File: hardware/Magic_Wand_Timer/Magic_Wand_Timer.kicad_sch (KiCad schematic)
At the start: 21 parts, among them J1 Conn_01x03, J2 Conn_01x03, J3 Conn_01x03, J4 Conn_01x02, Q1 AS2302, U1 MPM3610GQV-Z, U2 NE555D

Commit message: adding vias to a couple of PCBs, magic wand PCB changes
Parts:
- removed J1, J2, J3: Conn_01x03, Useful Modifications:JST_XH_B3B-XH-A_1x03_P2.54mm_Vertical, symbol Connector_Generic:Conn_01x03
- removed R3: 100K, Resistor_SMD:R_0805_2012Metric, symbol Device:R_Small
- removed U1: MPM3610GQV-Z, QFN3p0x5p0x1p6_MPM3610_MNP, symbol Magic_Wand_Timer:MPM3610GQV-Z
- added J1: Action Input, Connector_JST:JST_XH_B4B-XH-A_1x04_P2.50mm_Vertical, symbol Connector:Conn_01x04_Pin
- added J2: Caddy In/Out, Connector_JST:JST_XH_B4B-XH-A_1x04_P2.50mm_Vertical, symbol Connector:Conn_01x04_Pin
- added Q2: SI2301CDS-T1-GE3, Package_TO_SOT_SMD:SOT-23, symbol Transistor_FET:Si2371EDS
- added R7, R8: 100K, Resistor_SMD:R_0805_2012Metric, symbol Device:R_Small
- C1: MPN (none) -> C1710
- C2: value 10uF -> 10nF; MPN (none) -> C1710
- C3: value 22uF -> 1uF; MPN (none) -> C28323
- C4: MPN (none) -> C15850
- D1: value 1N4448W -> 1N4148W; MPN (none) -> C81598
- J4: symbol Connector_Generic:Conn_01x02 -> Connector:Conn_01x02_Pin
- Q1: MPN (none) -> C20917
- R1: value 100K -> 10K; MPN (none) -> C17414
- R2: value 19.1K -> 1K; MPN (none) -> C11702
- R4, R6: MPN (none) -> C17414
- R5: MPN (none) -> C149504
- U2: MPN (none) -> C7593
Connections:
- net +12V: now also J1.1 (Pin_1), J2.1 (Pin_1); no longer C2.1
- net +5V: now also J1.2 (Pin_2), J2.2 (Pin_2), Q2.2 (S), R8.1; no longer C3.1, R1.1
- net GND: now also C2.1, C3.1, J1.3 (Pin_3), J2.3 (Pin_3), R7.2; no longer C2.2, C3.2
- net Trigger: now also R1.1, R2.1, J1.4 (Pin_4); no longer R4.2, U2.2 (TR)
- net Filtered_Input: now reaches R1.2
- net Filtered_Input: now also C2.2, C3.2, R4.2, U2.2 (TR); no longer R2.1
- net at R2.2: now also Q2.1 (G), R8.2
- new net Caddy_Trigger: J2.4 (Pin_4), Q2.3 (D), R7.1
- no-connect marks 2 -> 1
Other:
- note removed: "DC-DC Converter"
- moved on the sheet: C1, C4, H1, H2, R4, R5, RV1, U2

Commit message: magic wand PCB updates
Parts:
- R1: renamed from R2; MPN C11702 -> C17513
- R4: value 10K -> 100K; MPN C17414 -> C149504
- renumbered C3 to C2, C2 to C3, J4 to J3, Q2 to Q1, Q1 to Q2, R8 to R2, R7 to R3, R1 to R5, R5 to R6, R6 to R7, U2 to U1
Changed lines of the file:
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@@
   (symbol (lib_id "Device:R_Small") (at 214.63 128.27 0) (unit 1)
     (in_bom yes) (on_board yes) (dnp no) (fields_autoplaced)
-    (property "Reference" "R6" (at 217.17 126.9999 0)
+    (property "Reference" "R7" (at 217.17 126.9999 0)
       (effects (font (size 1.27 1.27)) (justify left))
     )
@@
       (project "Magic_Wand_Timer"
         (path "/c5eed718-a5cc-419c-bfa3-9985e5d26a34"
-          (reference "R6") (unit 1)
+          (reference "R7") (unit 1)
         )
       )
@@
   (symbol (lib_id "Device:R_Small") (at 78.74 111.76 0) (unit 1)
     (in_bom yes) (on_board yes) (dnp no) (fields_autoplaced)
-    (property "Reference" "R7" (at 81.28 110.4899 0)
+    (property "Reference" "R3" (at 81.28 110.4899 0)
       (effects (font (size 1.27 1.27)) (justify left))
     )
@@
       (project "Magic_Wand_Timer"
         (path "/c5eed718-a5cc-419c-bfa3-9985e5d26a34"
-          (reference "R7") (unit 1)
+          (reference "R3") (unit 1)
         )
       )
@@
   (symbol (lib_id "Device:R_Small") (at 135.255 50.165 90) (unit 1)
     (in_bom yes) (on_board yes) (dnp no) (fields_autoplaced)
-    (property "Reference" "R1" (at 135.255 45.085 90)
+    (property "Reference" "R5" (at 135.255 45.085 90)
       (effects (font (size 1.27 1.27)))
     )
@@
       (project "Magic_Wand_Timer"
         (path "/c5eed718-a5cc-419c-bfa3-9985e5d26a34"
-          (reference "R1") (unit 1)
+          (reference "R5") (unit 1)
         )
       )
@@
   (symbol (lib_id "Transistor_FET:Si2371EDS") (at 76.2 97.155 0) (mirror x) (unit 1)
     (in_bom yes) (on_board yes) (dnp no)
-    (property "Reference" "Q2" (at 82.55 97.79 0)
+    (property "Reference" "Q1" (at 82.55 97.79 0)
       (effects (font (size 1.27 1.27)) (justify left))
     )
@@
       (project "Magic_Wand_Timer"
         (path "/c5eed718-a5cc-419c-bfa3-9985e5d26a34"
+          (reference "Q1") (unit 1)
+        )
+      )
+    )
+  )
+  (symbol (lib_id "Device:Q_NMOS_GSD") (at 223.52 123.19 0) (unit 1)
+    (in_bom yes) (on_board yes) (dnp no) (fields_autoplaced)
+    (property "Reference" "Q2" (at 229.87 121.9199 0)
+      (effects (font (size 1.27 1.27)) (justify left))
+    )
+    (property "Value" "AS2302" (at 229.87 124.4599 0)
+      (effects (font (size 1.27 1.27)) (justify left))
+    )
+    (property "Footprint" "Package_TO_SOT_SMD:SOT-23" (at 228.6 120.65 0)
+      (effects (font (size 1.27 1.27)) hide)
+    )
+    (property "Datasheet" "https://media.digikey.com/pdf/Data%20Sheets/Anbon%20Semi%20PDFs/AS2302.pdf" (at 223.52 123.19 0)
+      (effects (font (size 1.27 1.27)) hide)
+    )
+    (property "MPN" "C20917" (at 223.52 123.19 0)
+      (effects (font (size 1.27 1.27)) hide)
+    )
+    (pin "1")
+    (pin "2")
+    (pin "3")
+    (instances
+      (project "Magic_Wand_Timer"
+        (path "/c5eed718-a5cc-419c-bfa3-9985e5d26a34"
           (reference "Q2") (unit 1)
-        )
-      )
-    )
-  )
-  (symbol (lib_id "Device:Q_NMOS_GSD") (at 223.52 123.19 0) (unit 1)
-    (in_bom yes) (on_board yes) (dnp no) (fields_autoplaced)
-    (property "Reference" "Q1" (at 229.87 121.9199 0)
-      (effects (font (size 1.27 1.27)) (justify left))
-    )
-    (property "Value" "AS2302" (at 229.87 124.4599 0)
-      (effects (font (size 1.27 1.27)) (justify left))
-    )
-    (property "Footprint" "Package_TO_SOT_SMD:SOT-23" (at 228.6 120.65 0)
-      (effects (font (size 1.27 1.27)) hide)
-    )
-    (property "Datasheet" "https://media.digikey.com/pdf/Data%20Sheets/Anbon%20Semi%20PDFs/AS2302.pdf" (at 223.52 123.19 0)
-      (effects (font (size 1.27 1.27)) hide)
-    )
-    (property "MPN" "C20917" (at 223.52 123.19 0)
-      (effects (font (size 1.27 1.27)) hide)
-    )
-    (pin "1")
-    (pin "2")
-    (pin "3")
-    (instances
-      (project "Magic_Wand_Timer"
-        (path "/c5eed718-a5cc-419c-bfa3-9985e5d26a34"
-          (reference "Q1") (unit 1)
         )
       )
@@
   (symbol (lib_id "Device:R_Small") (at 173.99 91.44 0) (unit 1)
     (in_bom yes) (on_board yes) (dnp no) (fields_autoplaced)
-    (property "Reference" "R5" (at 176.53 90.1699 0)
+    (property "Reference" "R6" (at 176.53 90.1699 0)
       (effects (font (size 1.27 1.27)) (justify left))
     )
@@
       (project "Magic_Wand_Timer"
         (path "/c5eed718-a5cc-419c-bfa3-9985e5d26a34"
-          (reference "R5") (unit 1)
+          (reference "R6") (unit 1)
         )
       )
@@
   (symbol (lib_id "Device:C_Small") (at 143.51 55.88 180) (unit 1)
     (in_bom yes) (on_board yes) (dnp no)
-    (property "Reference" "C3" (at 146.05 55.88 90)
+    (property "Reference" "C2" (at 146.05 55.88 90)
       (effects (font (size 1.27 1.27)))
     )
@@
       (project "Magic_Wand_Timer"
         (path "/c5eed718-a5cc-419c-bfa3-9985e5d26a34"
-          (reference "C3") (unit 1)
+          (reference "C2") (unit 1)
         )
       )
@@
   (symbol (lib_id "Device:C_Small") (at 153.035 55.88 180) (unit 1)
     (in_bom yes) (on_board yes) (dnp no)
-    (property "Reference" "C2" (at 155.575 55.88 90)
+    (property "Reference" "C3" (at 155.575 55.88 90)
       (effects (font (size 1.27 1.27)))
     )
@@
       (project "Magic_Wand_Timer"
         (path "/c5eed718-a5cc-419c-bfa3-9985e5d26a34"
-          (reference "C2") (unit 1)
+          (reference "C3") (unit 1)
         )
       )
@@
   (symbol (lib_id "Device:R_Small") (at 69.85 92.71 0) (unit 1)
     (in_bom yes) (on_board yes) (dnp no)
-    (property "Reference" "R8" (at 65.405 90.805 0)
+    (property "Reference" "R2" (at 65.405 90.805 0)
       (effects (font (size 1.27 1.27)) (justify left))
     )
@@
       (project "Magic_Wand_Timer"
         (path "/c5eed718-a5cc-419c-bfa3-9985e5d26a34"
-          (reference "R8") (unit 1)
+          (reference "R2") (unit 1)
         )
       )
@@
   (symbol (lib_id "Timer:NE555D") (at 143.51 110.49 0) (unit 1)
     (in_bom yes) (on_board yes) (dnp no) (fields_autoplaced)
-    (property "Reference" "U2" (at 145.5294 97.79 0)
-      (effects (font (size 1.27 1.27)) (justify left))
-    )
-    (property "Value" "NE555D" (at 145.5294 100.33 0)
+    (property "Reference" "U1" (at 145.7041 97.79 0)
+      (effects (font (size 1.27 1.27)) (justify left))
+    )
+    (property "Value" "NE555D" (at 145.7041 100.33 0)
       (effects (font (size 1.27 1.27)) (justify left))
     )
@@
       (project "Magic_Wand_Timer"
         (path "/c5eed718-a5cc-419c-bfa3-9985e5d26a34"
-          (reference "U2") (unit 1)
+          (reference "U1") (unit 1)
         )
       )
@@
   (symbol (lib_id "Device:R_Small") (at 62.865 97.155 90) (unit 1)
     (in_bom yes) (on_board yes) (dnp no)
-    (property "Reference" "R2" (at 62.865 99.06 90)
+    (property "Reference" "R1" (at 62.865 99.06 90)
       (effects (font (size 1.27 1.27)))
     )
@@
       (effects (font (size 1.27 1.27)) hide)
     )
-    (property "MPN" "C11702" (at 62.865 97.155 90)
-      (effects (font (size 1.27 1.27)) hide)
-    )
-    (pin "1")
-    (pin "2")
-    (instances
-      (project "Magic_Wand_Timer"
-        (path "/c5eed718-a5cc-419c-bfa3-9985e5d26a34"
-          (reference "R2") (unit 1)
+    (property "MPN" "C17513" (at 62.865 97.155 90)
+      (effects (font (size 1.27 1.27)) hide)
+    )
+    (pin "1")
+    (pin "2")
+    (instances
+      (project "Magic_Wand_Timer"
+        (path "/c5eed718-a5cc-419c-bfa3-9985e5d26a34"
+          (reference "R1") (unit 1)
         )
       )
@@
       (effects (font (size 1.27 1.27)) (justify left))
     )
-    (property "Value" "10K" (at 130.81 100.3299 0)
+    (property "Value" "100K" (at 130.81 100.3299 0)
       (effects (font (size 1.27 1.27)) (justify left))
     )
@@
       (effects (font (size 1.27 1.27)) hide)
     )
-    (property "MPN" "C17414" (at 128.27 99.06 0)
+    (property "MPN" "C149504" (at 128.27 99.06 0)
       (effects (font (size 1.27 1.27)) hide)
     )
@@
   (symbol (lib_id "Connector:Conn_01x02_Pin") (at 233.68 115.57 180) (unit 1)
     (in_bom yes) (on_board yes) (dnp no)
-    (property "Reference" "J4" (at 234.95 114.935 0)
+    (property "Reference" "J3" (at 234.95 114.935 0)
       (effects (font (size 1.27 1.27)) (justify right))
     )
@@
       (project "Magic_Wand_Timer"
         (path "/c5eed718-a5cc-419c-bfa3-9985e5d26a34"
-          (reference "J4") (unit 1)
-        )
-      )
+          (reference "J3") (unit 1)
+        )
+      )

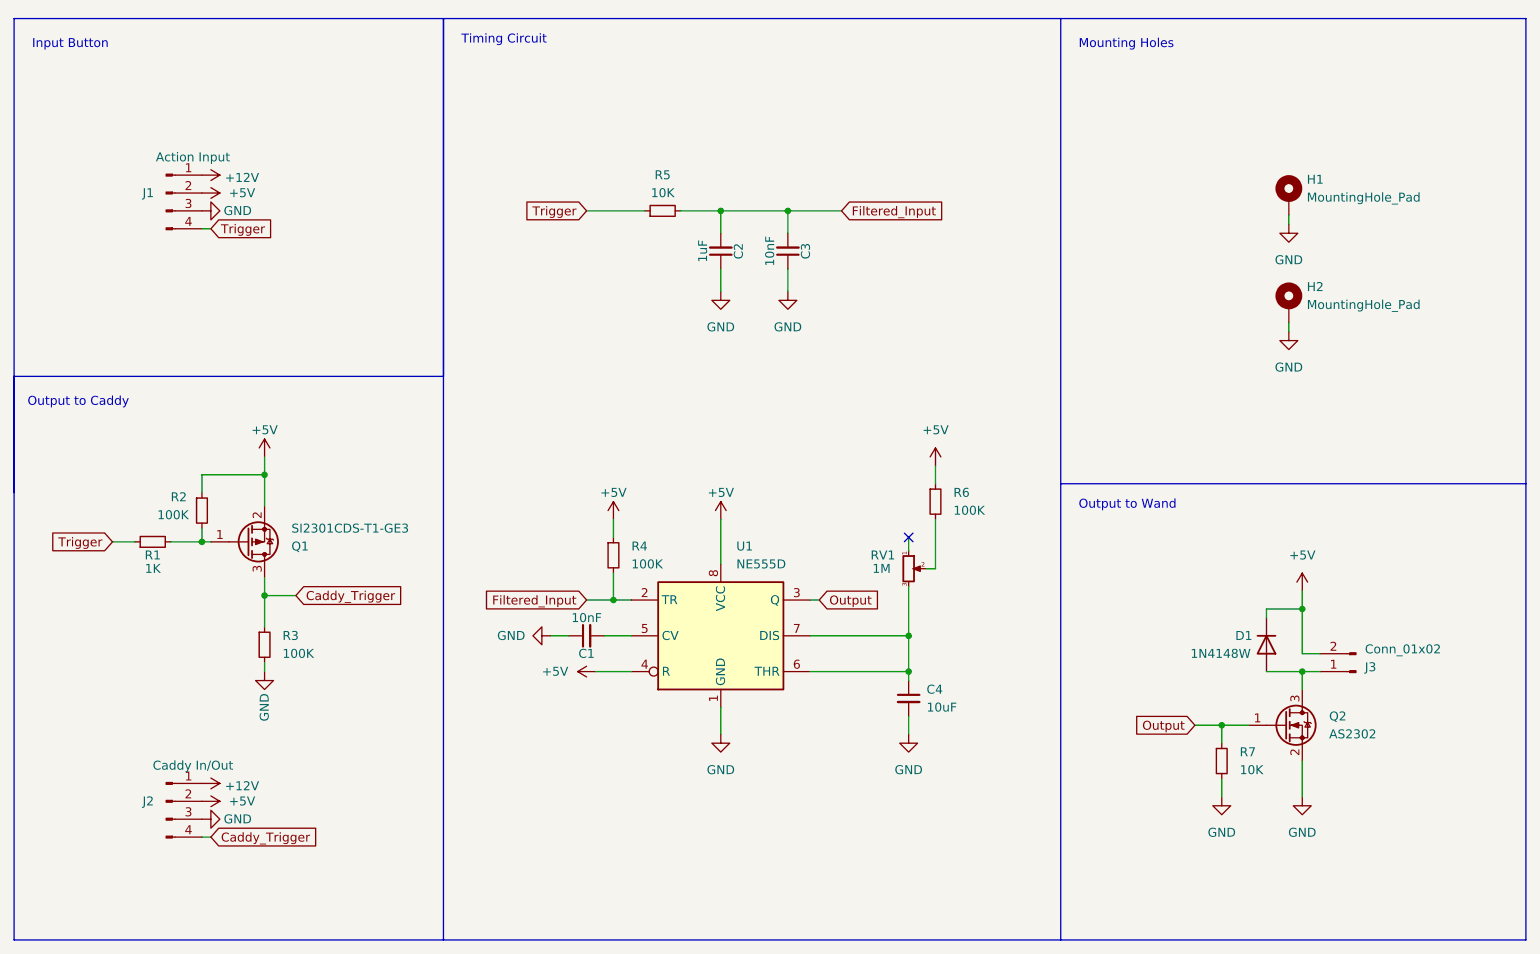
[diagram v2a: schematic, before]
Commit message: Magic Wand Timer Updates
Added 12V/5V switching, SMD/THT potentiometer options, Delayed start to handle erratic comparator behavior
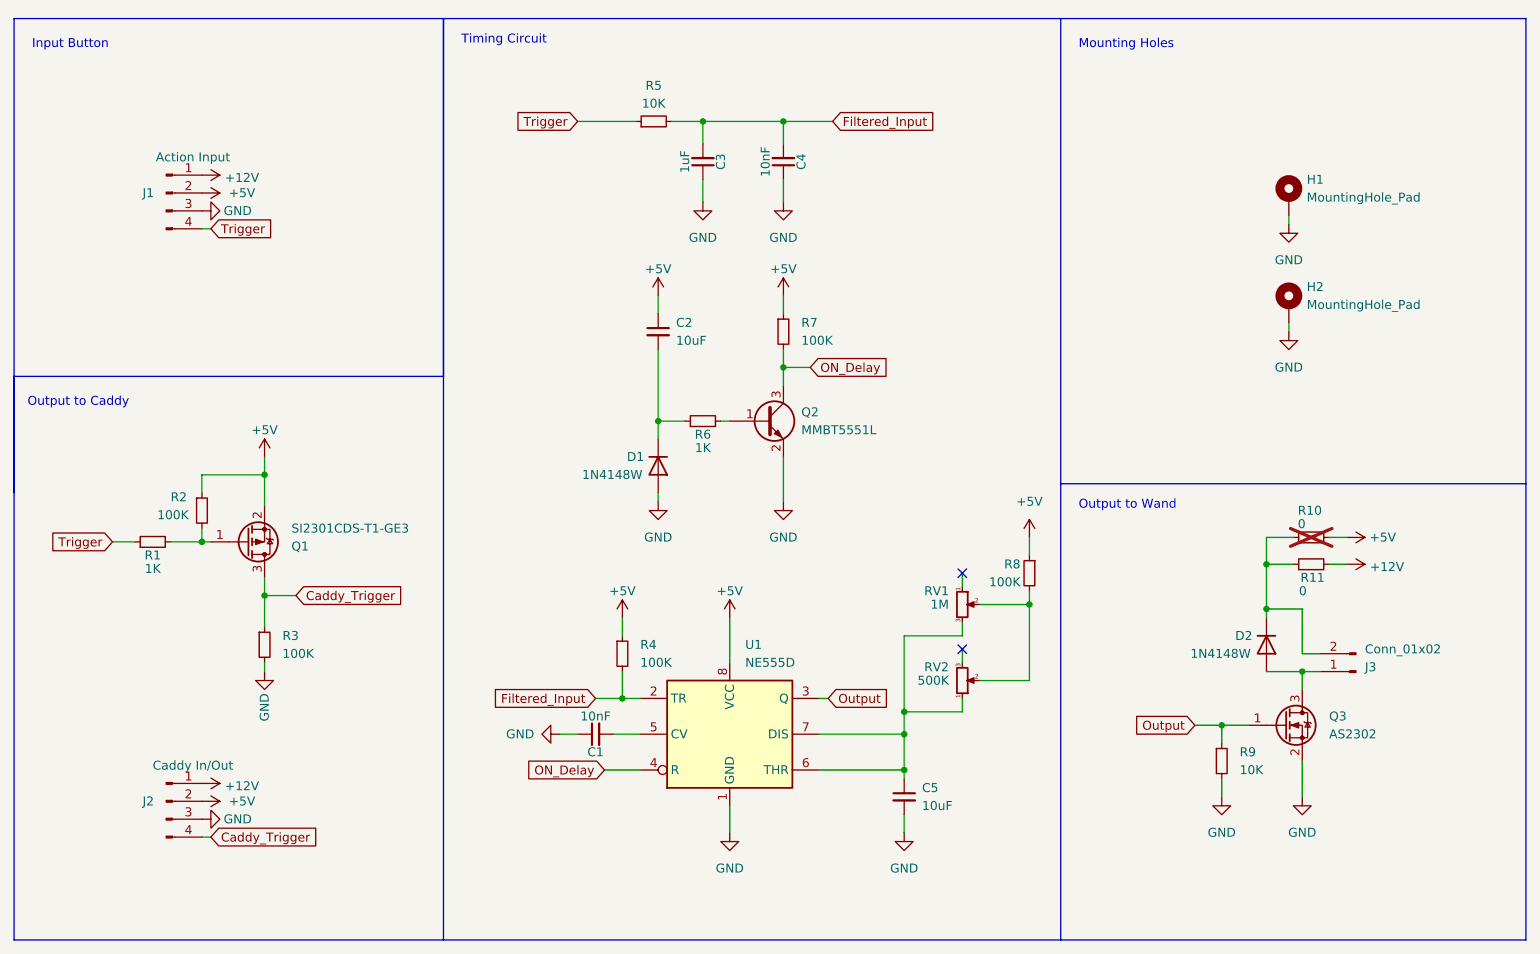
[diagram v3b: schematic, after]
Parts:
- added C2: 10uF, Capacitor_SMD:C_0805_2012Metric, symbol Device:C_Small
- added D1: 1N4148W, Diode_SMD:D_SOD-123, symbol Diode:1N4448W
- added Q2: MMBT5551L, Package_TO_SOT_SMD:SOT-23, symbol Transistor_BJT:MMBT5551L
- added R10, R11: 0, Resistor_SMD:R_0805_2012Metric, symbol Device:R_Small
- added R6: 1K, Resistor_SMD:R_0805_2012Metric, symbol Device:R_Small
- added R7: 100K, Resistor_SMD:R_0805_2012Metric, symbol Device:R_Small
- added RV2: 500K, Potentiometer_SMD:Potentiometer_Bourns_TC33X_Vertical, symbol Device:R_Potentiometer_Small
- renumbered C2 to C3, C3 to C4, C4 to C5, D1 to D2, Q2 to Q3, R6 to R8, R7 to R9
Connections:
- net +12V: now also R11.2
- net +5V: now also C2.1, R10.1, R7.1; no longer D2.1 (K), J3.2 (Pin_2), U1.4 (R)
- net GND: now also D1.2 (A), Q2.2 (E)
- net at R8.2, RV1.2: now also RV2.2
- net at C5.1, RV1.3, U1.6 (THR)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: now also RV2.1
- new net: Q2.1 (B), R6.2
- new net: C2.2, D1.1 (K), R6.1
- new net: D2.1 (K), J3.2 (Pin_2), R10.2, R11.1
- new net ON_Delay: Q2.3 (C), R7.2, U1.4 (R)
- no-connect marks 1 -> 2
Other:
- moved on the sheet: C1, C3, C4, C5, R4, R5, R8, RV1, U1

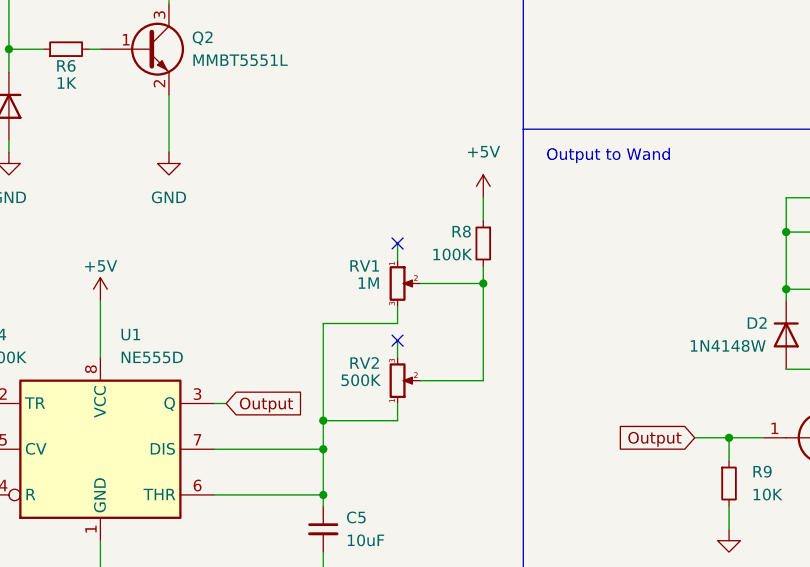
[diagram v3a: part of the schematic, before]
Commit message: Wand Timer V3 Routing
Finished routing components for V3 Magic Wand Timer
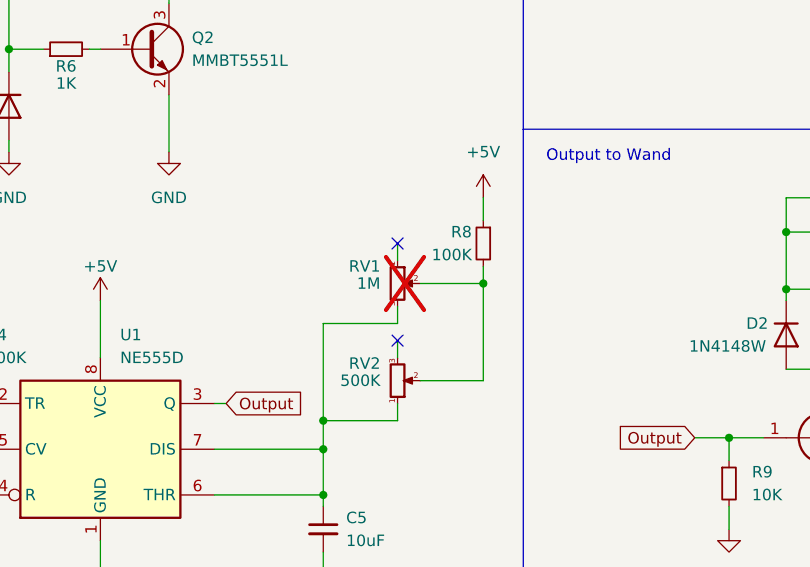
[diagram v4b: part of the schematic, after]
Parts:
- RV1: now not fitted
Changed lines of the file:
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@@
   )
   (symbol (lib_id "Device:R_Potentiometer_Small") (at 177.8 106.045 0) (unit 1)
-    (in_bom yes) (on_board yes) (dnp no)
+    (in_bom yes) (on_board yes) (dnp yes)
     (property "Reference" "RV1" (at 175.895 104.14 0)
       (effects (font (size 1.27 1.27)) (justify right))
